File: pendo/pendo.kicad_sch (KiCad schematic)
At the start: 35 parts, among them J1 M2, J2 M1, J3 Motor Vin, J4 Conn_ARM_JTAG_SWD_10, SW1 SW_Push, U1 STM32G431RBTx, U10 DRV8231ADSG, U11 DRV8231ADSG, U4 ESP32-C3-WROOM-02, U5 AP2112K-3.3, U9 RPX-2.5-CT

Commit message: cleaning up pendulum schematic
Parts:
- added C16, C17: 0.1u, symbol Device:C
- added R7: 4.7k, symbol Device:R_US
- added U2: LSM6DS3, Package_LGA:LGA-14_3x2.5mm_P0.5mm_LayoutBorder3x4y, symbol Sensor_Motion:LSM6DS3
- R1, R2: value 0.2 -> 1.5k
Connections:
- net +12V: now also C10.2, C11.2, C9.2, U10.5 (VM), U11.5 (VM)
- net +3.3V: now also C16.1, C17.1, R7.1, U2.1 (SDO/SA0), U2.2 (SDX), U2.3 (SCX), U2.5 (VDDIO), U2.8 (VDD); no longer R4.2, U9.3 (VOUT)
- net GND: now also C10.1, C11.1, C8.1, C9.1, J4.10 (~{RESET}), R1.1, R2.1, SW1.1, U1.7 (PG10), U4.3 (IO4), C16.2, C17.2, U2.6 (GND), U2.7 (GND); no longer C10.2, C11.2, C9.2, R1.2, R2.2
- net VPROPI1: now reaches U10.1 (IPROPI)
- net VPROPI1: now also R1.2, U1.25 (PB1); no longer R1.1
- net TIM1_2: now reaches U1.9 (PC1), U10.2 (IN2)
- net TIM1_1: now reaches U1.8 (PC0), U10.3 (IN1)
- net I2C3_SDA: now reaches U6.1 (P1), U7.1 (P1), U8.1 (P1)
- net I2C3_SDA: now also U1.41 (PC9), U2.14 (SDA); no longer U1.40 (PC8)
- net I2C3_SCL: now reaches U6.2 (P2), U7.2 (P2), U8.2 (P2)
- net I2C3_SCL: now also U1.40 (PC8), U2.13 (SCL); no longer U1.41 (PC9)
- net VPROPI2: now reaches U11.1 (IPROPI)
- net VPROPI2: now also R2.2, U1.26 (PB2); no longer R2.1
- net JDB_SWDIO: now reaches J4.2 (SWDIO/TMS)
- net JDB_SWDIO: now also U4.15 (IO3)
- net JDB_SWCLK: now reaches J4.4 (SWCLK/TCK)
- net JDB_SWCLK: now also U4.16 (IO2)
- net TIM1_3: now reaches U1.10 (PC2), U11.3 (IN1)
- net TIM1_4: now reaches U1.11 (PC3), U11.2 (IN2)
- net ESP32_RX: now reaches U1.14 (PA2)
- net ESP32_RX: now also U4.11 (IO20/RXD)
- net ESP32_TX: now reaches U1.17 (PA3)
- net ESP32_TX: now also U4.12 (IO21/TXD)
- net IMU_INT: now reaches U1.22 (PC4)
- net IMU_INT: now also U2.4 (INT1)
- new net: R7.2, U2.12 (CS)
- new net +5V: C13.1, R4.2, U5.1 (VIN), U5.3 (EN), U9.3 (VOUT)
- no-connect marks 0 -> 52
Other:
- moved on the sheet: C1, C12, C13, C2, C3, C4, C5, C6, C7, C8, J2, J4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

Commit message: cleaned up schematic
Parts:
- removed J3: Motor Vin, TerminalBlock:TerminalBlock_MaiXu_MX126-5.0-02P_1x02_P5.00mm, symbol Connector:Screw_Terminal_01x02
- added R8, R9: 4.7k, symbol Device:R_US
- R6: value R_US -> 2.2k
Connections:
- net +3.3V: now also R8.1, R9.1
- net GND: no longer C8.1, J4.10 (~{RESET}), SW1.1, U1.7 (PG10), U4.3 (IO4)
- net I2C3_SCL: now also R8.2
- net I2C3_SDA: now also R9.2
- net JDB_SWCLK: now also U1.50 (PA14)
- net JDB_SWDIO: now also U1.49 (PA13)
- new net JDB_RESET: C8.1, J4.10 (~{RESET}), SW1.1, U1.7 (PG10), U4.3 (IO4)
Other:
- note added: "Buck Converter 12V->5V"
- note added: "Buck Converter Decoupling"
- note added: "ESP32 Wireless transceiver"
- note added: "I2C Headers"
- note added: "I2C Pullups"
- note added: "IMU"
- note added: "IMU Decoupling"
- note added: "JTAG Debug Header"
- note added: "LDO Regulator"
- note added: "MCU1"
- note added: "Motor DRV1"
- note added: "Motor DRV2"
- note added: "Motor Driver Decoupling"
- note added: "Reset Button"
- note added: "STM32 Decoupling"
- moved on the sheet: C1, C10, C11, C12, C13, C14, C15, C16, C17, C2, C3, C4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

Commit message: finished schematic
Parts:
- removed J1: M2, TerminalBlock:TerminalBlock_MaiXu_MX126-5.0-02P_1x02_P5.00mm, symbol Connector:Screw_Terminal_01x02
- removed J2: M1, TerminalBlock:TerminalBlock_MaiXu_MX126-5.0-02P_1x02_P5.00mm, symbol Connector:Screw_Terminal_01x02
- removed U6, U7, U8: (no value), Connector_PinHeader_2.54mm:PinHeader_1x02_P2.54mm_Vertical, symbol Terminals:2pin
- added C18: 47u, Capacitor_SMD:C_1206_3216Metric, symbol Device:C
- added C19, C21: 1u, symbol Device:C
- added C20, C22: 0.1u, symbol Device:C
- added FB1: FerriteBead_Small, symbol Device:FerriteBead_Small
- added J3, J5, J6: Conn_01x04_Pin, symbol Connector:Conn_01x04_Pin
- added J7: Conn_02x10_Odd_Even, symbol Connector_Generic:Conn_02x10_Odd_Even
- added J8, J9: Conn_01x06_Pin, symbol Connector:Conn_01x06_Pin
- added R10, R11: 4.7k, symbol Device:R_US
- added R12: 10k, symbol Device:R_US
- C5: footprint Capacitor_SMD:C_0603_1608Metric -> (none)
- R3: value 68.1k -> 10k
- R5: value 25.5k -> 3.3k
- R6: value 2.2k -> 1.37k
- R7: value 4.7k -> 10k
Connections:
- net +12V: now also C18.2, J7.1 (Pin_1), J7.2 (Pin_2)
- net +3.3V: now also FB1.2, J3.2 (Pin_2), J5.2 (Pin_2), J6.2 (Pin_2), J7.5 (Pin_5), J8.4 (Pin_4), J9.4 (Pin_4), R10.1, R11.1, R12.1; no longer C5.2, U1.29 (VDDA), U2.1 (SDO/SA0), U2.2 (SDX), U2.3 (SCX)
- net GND: now also C5.2, C18.1, C19.2, C20.2, C21.2, C22.2, J3.1 (Pin_1), J5.1 (Pin_1), J6.1 (Pin_1), J7.20 (Pin_20), J7.3 (Pin_3), J7.4 (Pin_4), J7.6 (Pin_6), J8.3 (Pin_3), J9.3 (Pin_3); no longer C5.1
- net I2C3_SCL: now also J3.4 (Pin_4), J5.4 (Pin_4), J6.4 (Pin_4); no longer U2.13 (SCL)
- net I2C3_SDA: now also J3.3 (Pin_3), J5.3 (Pin_3), J6.3 (Pin_3); no longer U2.14 (SDA)
- net JDB_RESET: now also J7.19 (Pin_19)
- net E_STOP: now reaches R7.2
- net E_STOP: now also U1.35 (PB13), J7.16 (Pin_16); no longer U2.12 (CS)
- net M1+: now reaches U10.6 (OUT1)
- net M1+: now also J8.1 (Pin_1)
- net M1-: now reaches U10.8 (OUT2)
- net M1-: now also J8.2 (Pin_2)
- net VBAT_PROTECT: now reaches R3.2, R5.1
- net VBAT_PROTECT: now also U1.24 (PB0); no longer U9.9 (CTRL)
- net ENC1A: now reaches U1.12 (PA0)
- net ENC1A: now also J8.5 (Pin_5)
- net ENC1B: now reaches U1.13 (PA1)
- net ENC1B: now also J8.6 (Pin_6)
- net ENC2B: now reaches U1.18 (PA4)
- net ENC2B: now also J9.6 (Pin_6)
- net SPI1_SCK: now reaches U1.19 (PA5)
- net SPI1_SCK: now also U2.3 (SCX), J7.13 (Pin_13)
- net SPI1_MISO: now reaches U1.20 (PA6)
- net SPI1_MISO: now also U2.1 (SDO/SA0), J7.12 (Pin_12)
- net SPI1_MOSI: now reaches U1.21 (PA7)
- net SPI1_MOSI: now also U2.2 (SDX), J7.11 (Pin_11)
- net +3.3VA: now reaches U1.28 (VREF+)
- net +3.3VA: now also U1.29 (VDDA), C19.1, C20.1, C21.1, C22.1, FB1.1
- net SPI1_GP_CS2: now reaches U1.30 (PB10)
- net SPI1_GP_CS2: now also J7.15 (Pin_15)
- net PB11: now reaches U1.33 (PB11)
- net PB11: now also J7.17 (Pin_17)
- net PB12: now reaches U1.34 (PB12)
- net PB12: now also J7.18 (Pin_18)
- net ENC2A: now reaches U1.38 (PC6)
- net ENC2A: now also J9.5 (Pin_5)
- net IMU_CS: now reaches U1.42 (PA8)
- net IMU_CS: now also U2.12 (CS)
- net USART3_TX: now reaches U1.52 (PC10)
- net USART3_TX: now also J7.7 (Pin_7)
- net USART3_RX: now reaches U1.53 (PC11)
- net USART3_RX: now also J7.8 (Pin_8)
- net I2C1_SDA: now reaches U1.60 (PB7)
- net I2C1_SDA: now also J7.9 (Pin_9), R11.2
- net I2C1_SCL: now reaches U1.61 (PB8)
- net I2C1_SCL: now also J7.10 (Pin_10), R10.2
- net SPI1_GP_CS1: now reaches U1.62 (PB9)
- net SPI1_GP_CS1: now also J7.14 (Pin_14)
- net at U4.2 (EN): now also C5.1, R12.2
- net M2+: now reaches U11.6 (OUT1)
- net M2+: now also J9.1 (Pin_1)
- net M2-: now reaches U11.8 (OUT2)
- net M2-: now also J9.2 (Pin_2)
- no-connect marks 52 -> 36
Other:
- note added: "Battery VSense"
- note added: "E stop pullup"
- note added: "Expansion Bus"
- note added: "STM32 Analog Decoupling"
- moved on the sheet: C1, C2, C3, C4, C6, R4, R6, U9

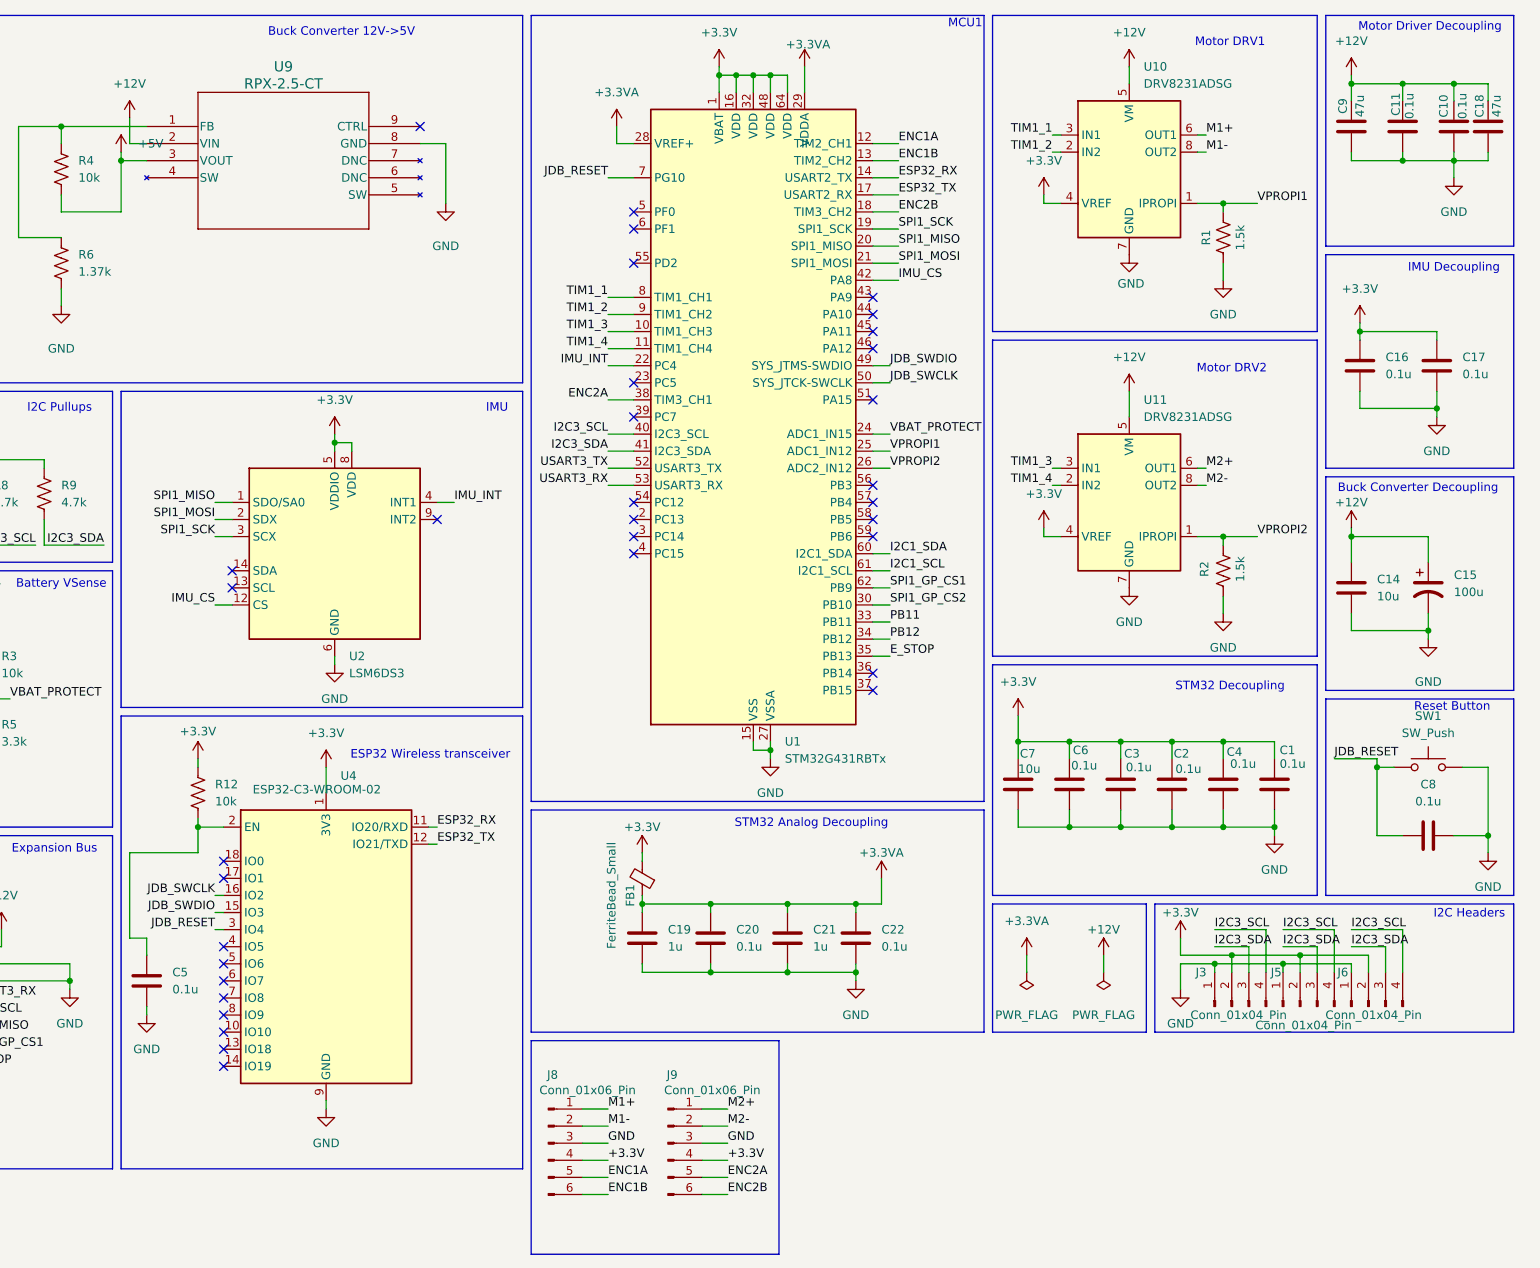
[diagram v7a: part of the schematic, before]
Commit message: added planes and almost finished routing
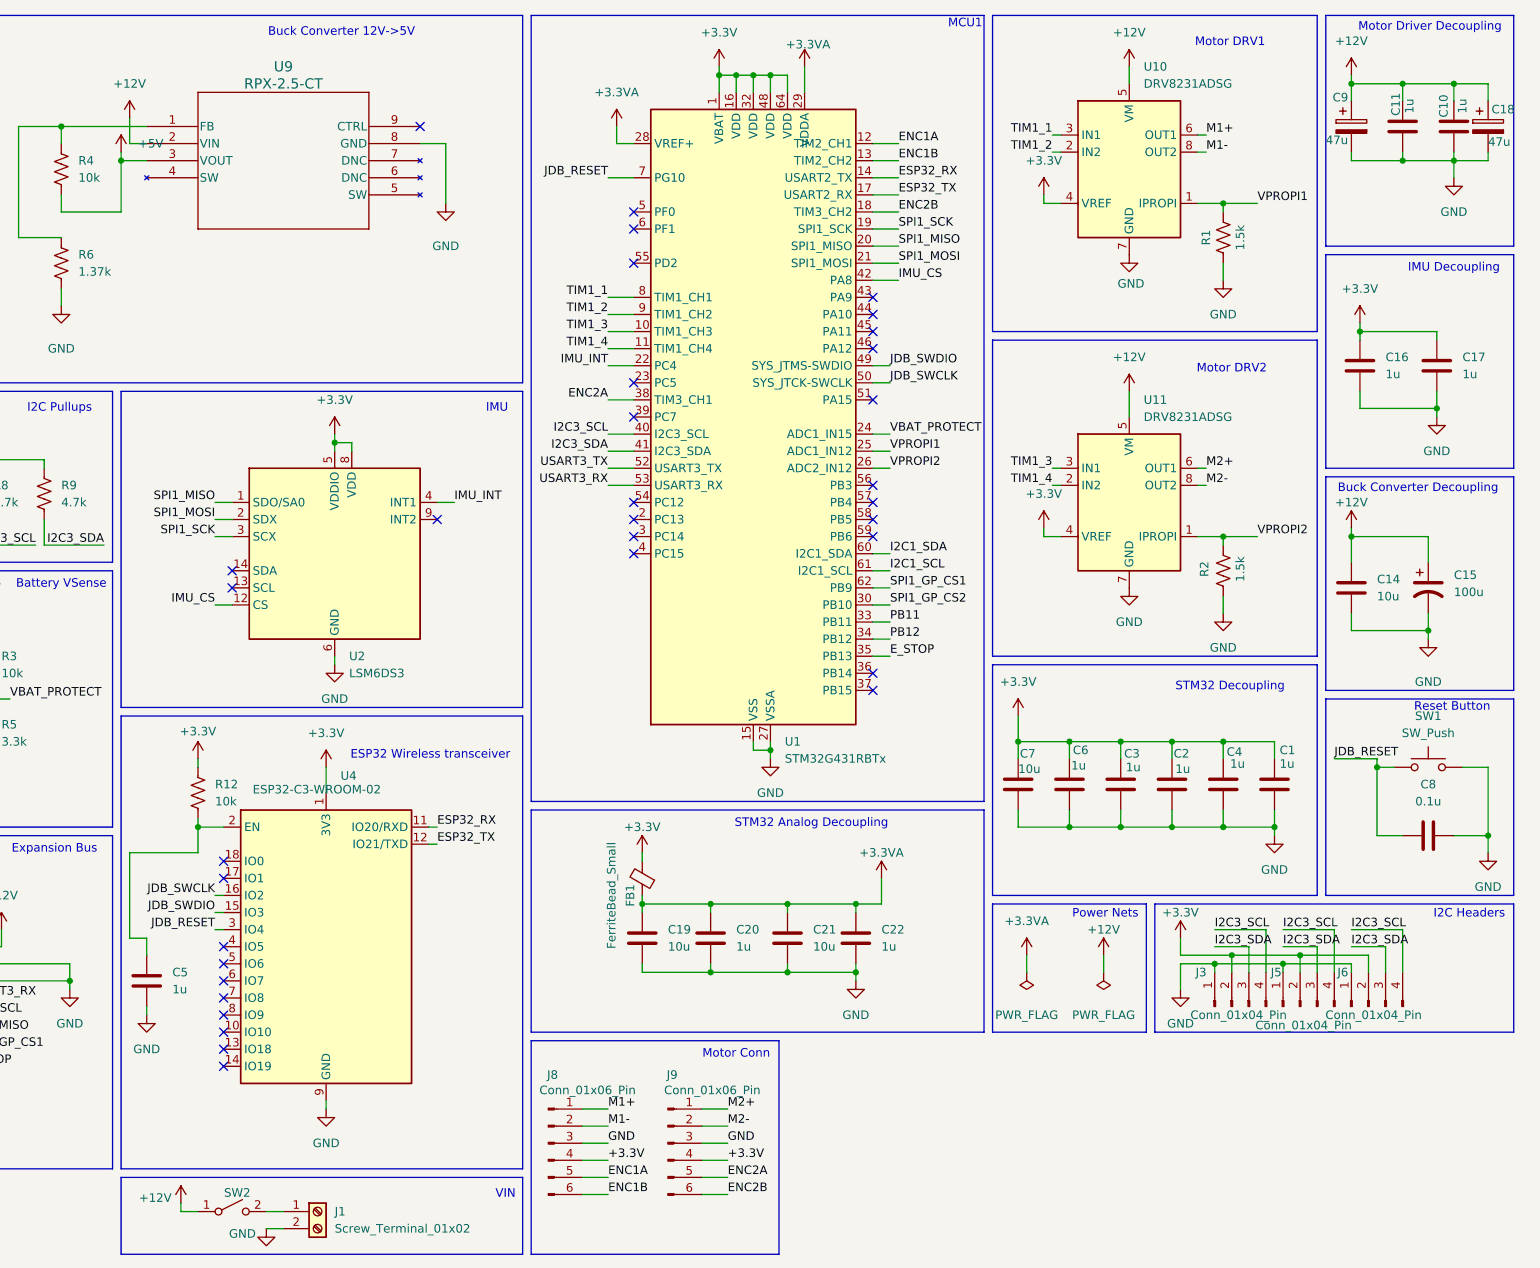
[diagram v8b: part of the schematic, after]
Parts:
- removed C18, C9: 47u, Capacitor_SMD:C_1206_3216Metric, symbol Device:C
- added C18, C9: 47u, Capacitor_SMD:CP_Elec_6.3x5.4, symbol Device:C_Polarized
- added J1: Screw_Terminal_01x02, TerminalBlock:TerminalBlock_MaiXu_MX126-5.0-02P_1x02_P5.00mm, symbol Connector:Screw_Terminal_01x02
- added SW2: SW_SPST, jlc:SWITCH HIGH VOLTAGE, symbol Switch:SW_SPST
- C1, C2, C3, C4, C6: value 0.1u -> 1u; footprint Capacitor_SMD:C_0603_1608Metric -> Capacitor_SMD:C_0402_1005Metric
- C10, C11: value 0.1u -> 1u; footprint Capacitor_SMD:C_1206_3216Metric -> Capacitor_SMD:C_0402_1005Metric
- C14: footprint (none) -> Capacitor_SMD:C_0805_2012Metric
- C15: footprint (none) -> Capacitor_SMD:CP_Elec_6.3x7.7
- C16, C17, C20, C22, C5: value 0.1u -> 1u; footprint (none) -> Capacitor_SMD:C_0402_1005Metric
- C19, C21: value 1u -> 10u; footprint (none) -> Capacitor_SMD:C_0805_2012Metric
- C8: footprint Capacitor_SMD:C_0603_1608Metric -> Capacitor_SMD:C_0402_1005Metric
- J3, J5, J6: footprint (none) -> Connector_PinHeader_2.54mm:PinHeader_1x04_P2.54mm_Vertical
- J7: footprint (none) -> Connector_IDC:IDC-Header_2x10_P2.54mm_Vertical
- J8, J9: footprint (none) -> Connector_JST:JST_XH_B6B-XH-AM_1x06_P2.50mm_Vertical
- R10, R11, R12, R7, R8, R9: footprint (none) -> Resistor_SMD:R_0402_1005Metric
- R3, R4, R5, R6: footprint (none) -> Resistor_SMD:R_0603_1608Metric
- U9: footprint RPX-2.5 -> (none)
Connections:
- net +12V: now also C18.1, C9.1, SW2.1 (A)
- net GND: now also C18.2, C9.2, J1.2 (Pin_2)
- new net: J1.1 (Pin_1), SW2.2 (B)
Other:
- note added: "Motor Conn"
- note added: "Power Nets"
- note added: "VIN"
